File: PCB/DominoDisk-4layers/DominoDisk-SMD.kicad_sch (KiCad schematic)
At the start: 28 parts, among them J1 Daisy port out, J2 ICSP_ISP6, J3 Daisy port in, J4 UART, K1 TF-104, U1 PC817C-S, U2 SE5218, U3 ATmega328P-AU, U4 TXB0104PWR, Y1 Resonator

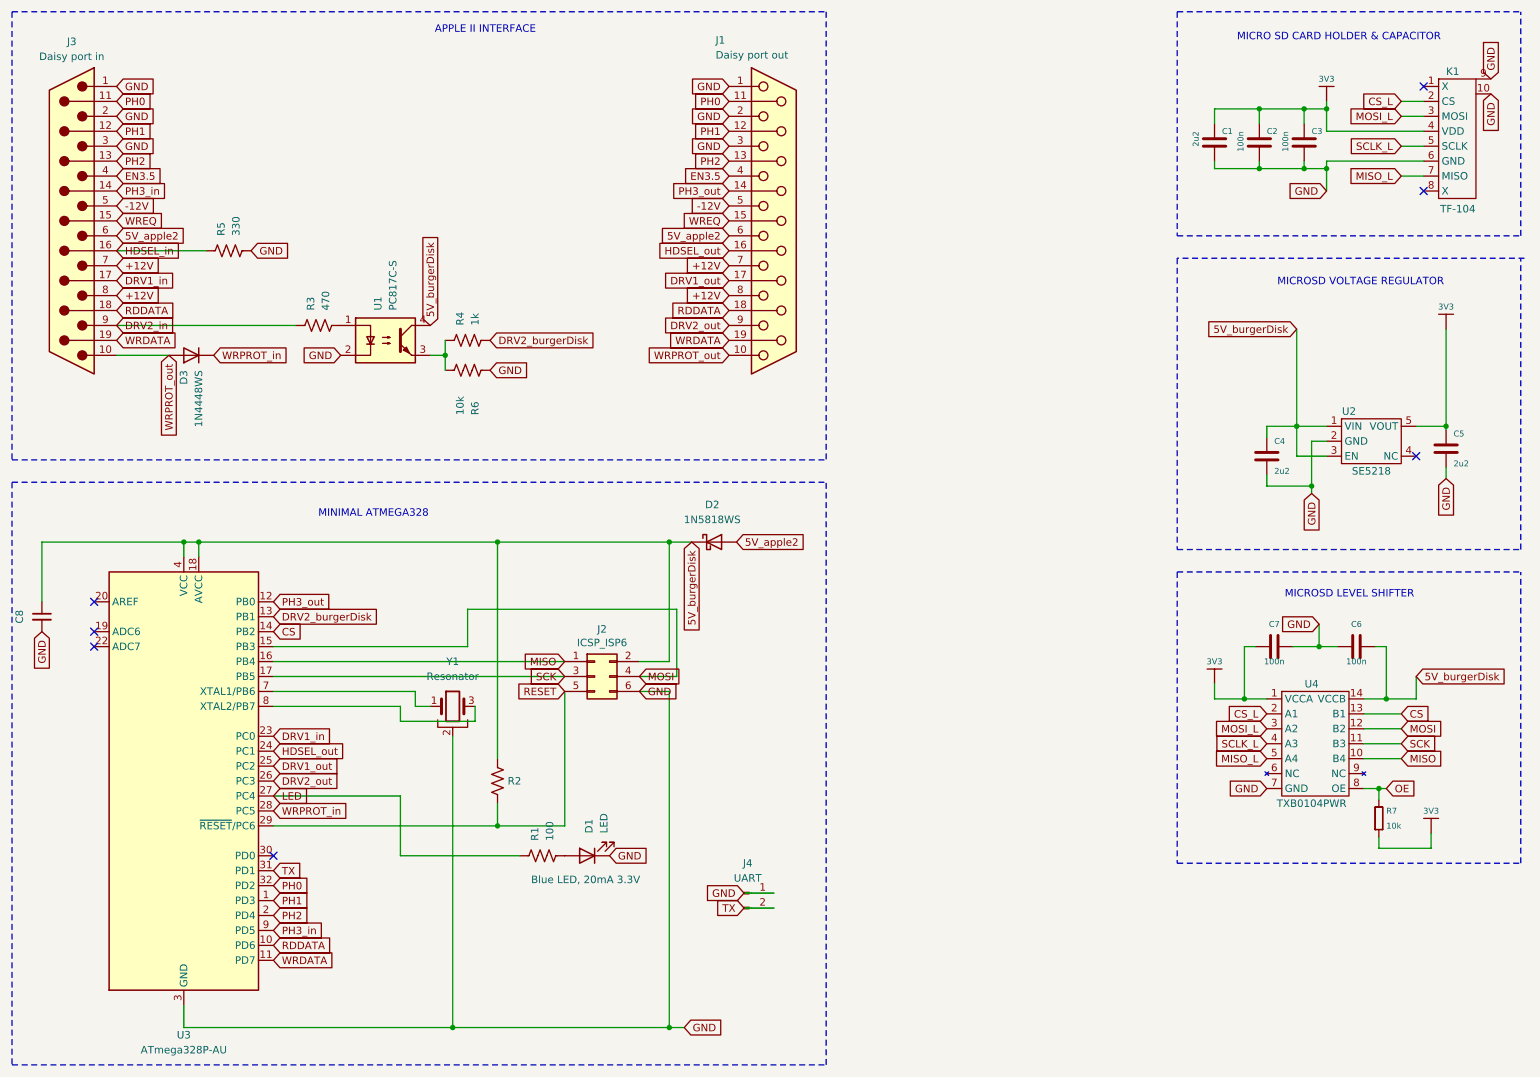
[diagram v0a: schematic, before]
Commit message: Fix microSD caps
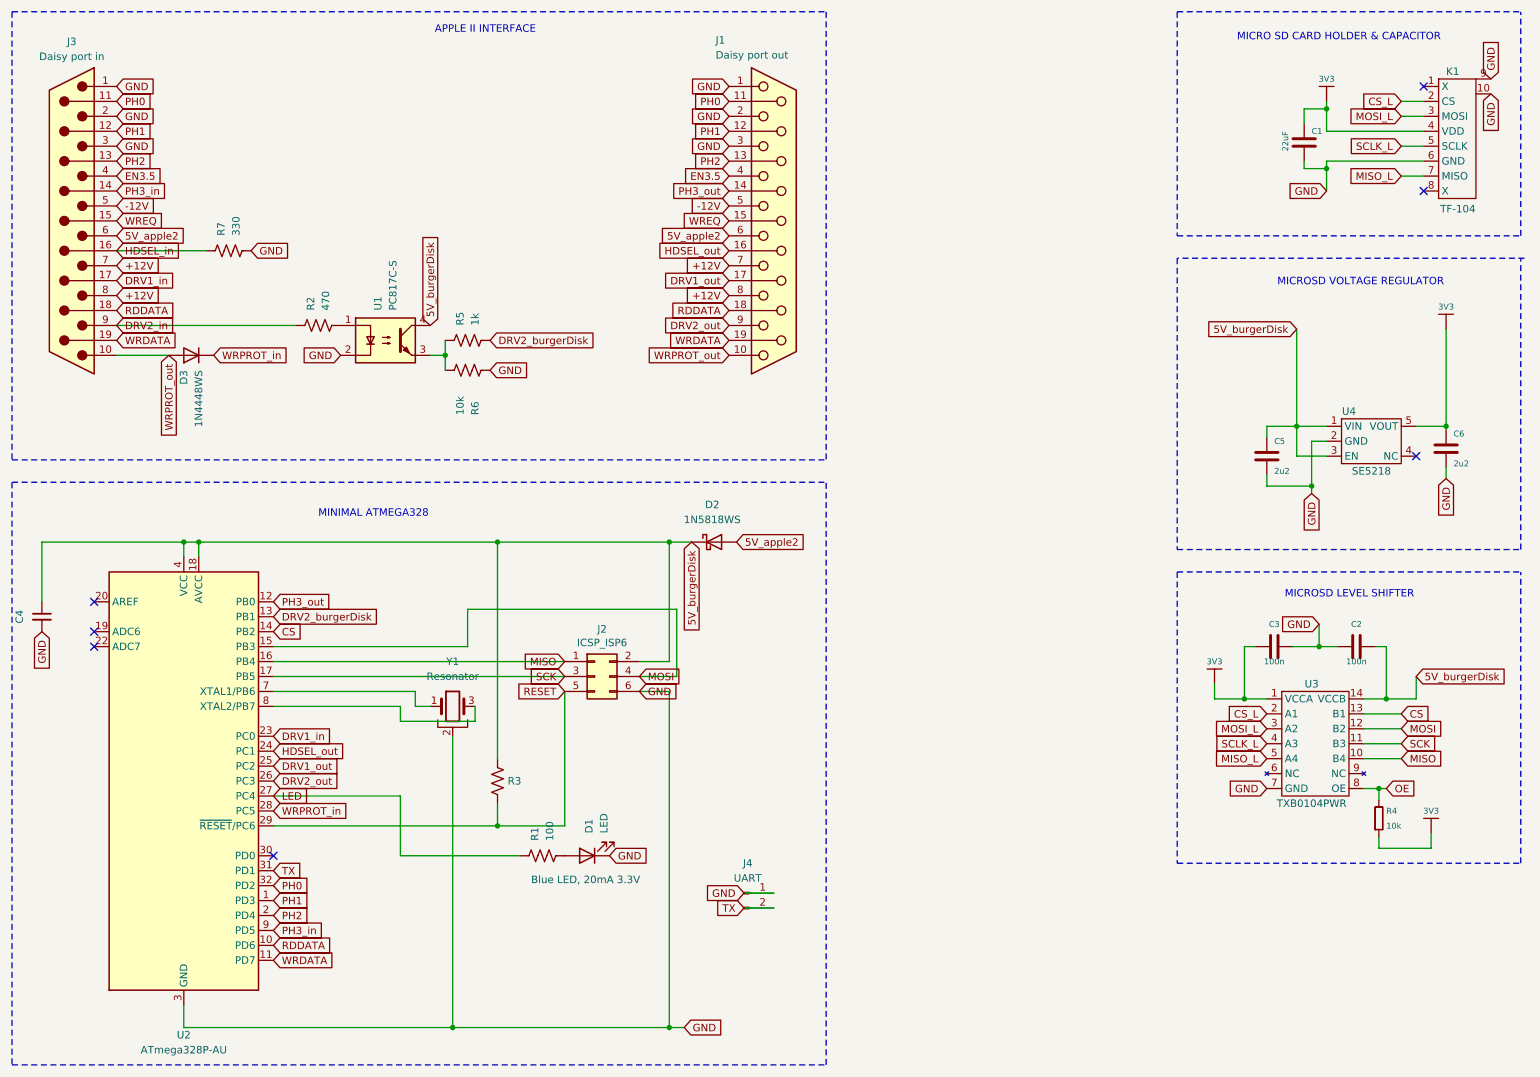
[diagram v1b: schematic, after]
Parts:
- removed C1: 2u2, Capacitor_SMD:C_0603_1608Metric, symbol e-radionica.com schematics:0603C
- removed C2: 100n, Capacitor_SMD:C_0603_1608Metric, symbol e-radionica.com schematics:0603C
- C1: renamed from C3; value 100n -> 22uF; footprint Capacitor_SMD:C_0603_1608Metric -> Capacitor_SMD:C_0805_2012Metric; LCSC C1590 -> C45783
- renumbered C6 to C2, C7 to C3, C8 to C4, C4 to C5, C5 to C6, R3 to R2, R2 to R3, R7 to R4, R4 to R5, R5 to R7, U3 to U2, U4 to U3, U2 to U4

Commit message: Small caps fixes
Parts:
- J4: footprint Connector_PinHeader_2.54mm:PinHeader_1x02_P2.54mm_Horizontal -> Connector_PinHeader_2.54mm:PinHeader_1x02_P2.54mm_Vertical
- K1: LCSC C341092 -> C266612
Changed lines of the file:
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@@
 			)
 		)
-		(property "Footprint" "Connector_PinHeader_2.54mm:PinHeader_1x02_P2.54mm_Horizontal"
+		(property "Footprint" "Connector_PinHeader_2.54mm:PinHeader_1x02_P2.54mm_Vertical"
 			(at 148.59 165.1 0)
 			(effects
@@
 			)
 		)
-		(property "LCSC" "C341092"
+		(property "LCSC" "C266612"
 			(at 269.24 36.83 0)
 			(effects
